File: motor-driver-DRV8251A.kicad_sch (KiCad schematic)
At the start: 7 parts, among them U3 DRV8251ADDAR, U4 INA139

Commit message: minor improvements
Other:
- note added: "DRV8251A Datasheet (driver): https://www.ti.com/lit/ds/symlink/drv8251a.pdf"
- note added: "Drive all motors using PWM signals. Additionally amplify the current sense value to something an ESP32 can measure. Capacitance values are taken directly from the datasheet."
- note added: "INA139 Datasheet (amplifier): https://www.ti.com/lit/ds/symlink/ina139.pdf"
- note added: "Motor Power Section"
- note added: "We assume 4 A max current, since the DRV8251A is rated for 4.1 A. So, a 10 milli-ohm resistor gives us a 40 mV drop. This is then amplified 24 times using a 24k resistor, giving us a theoretical voltage drop of 960 mV. The ESP32 has been tested to measure reliably up to 1 V on its built-in ADC. Resistor power lost = 160 mW."
- company: (none) -> Anuj Verma
- title: (none) -> DRV8251 Motor Driver
- moved on the sheet: C2, C3, C4, R17, R18, U3, U4

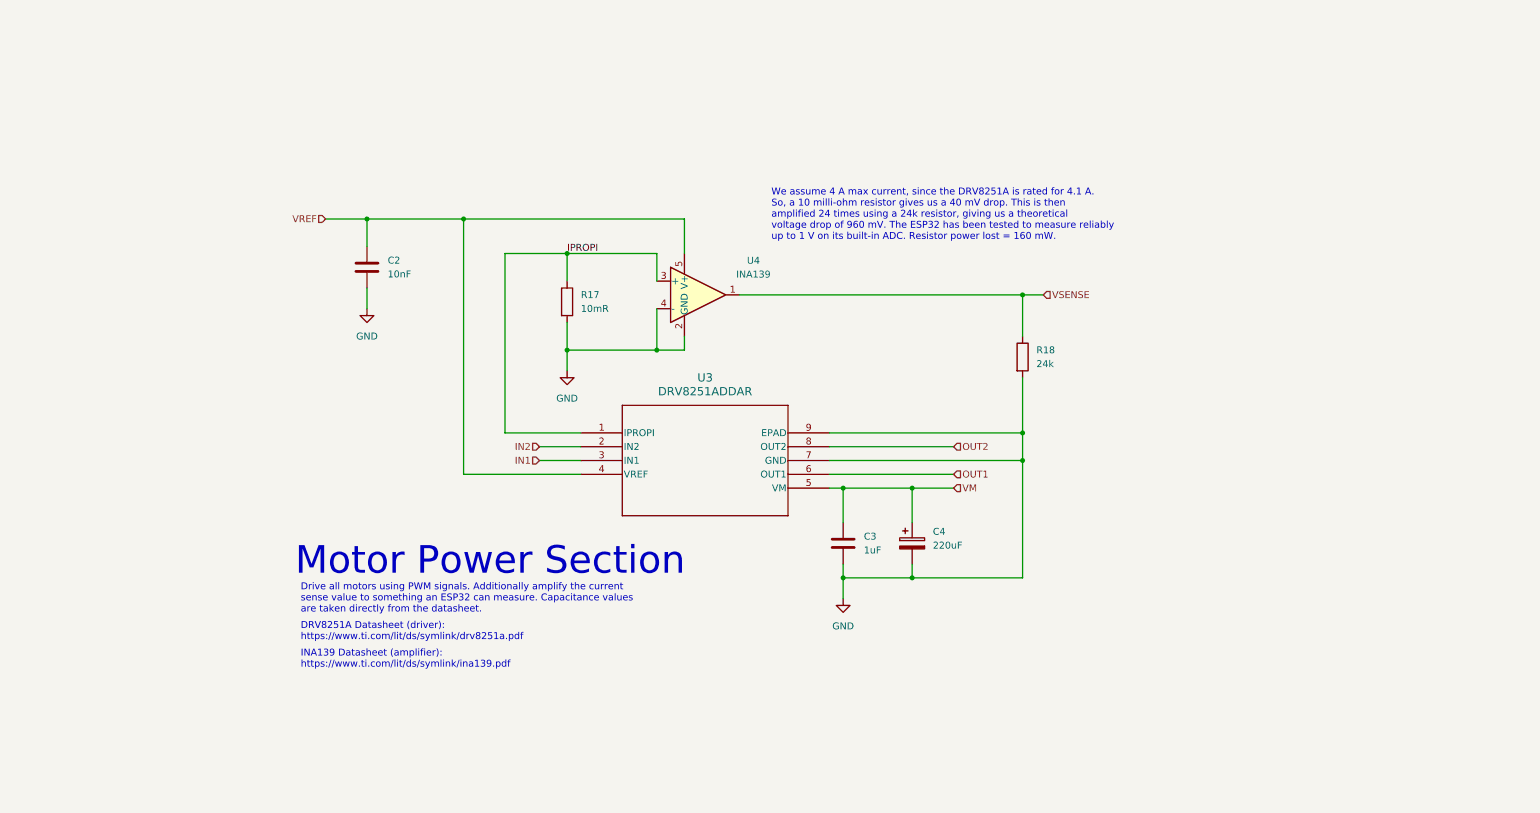
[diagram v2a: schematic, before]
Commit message: basic redesign. PCB not up to date
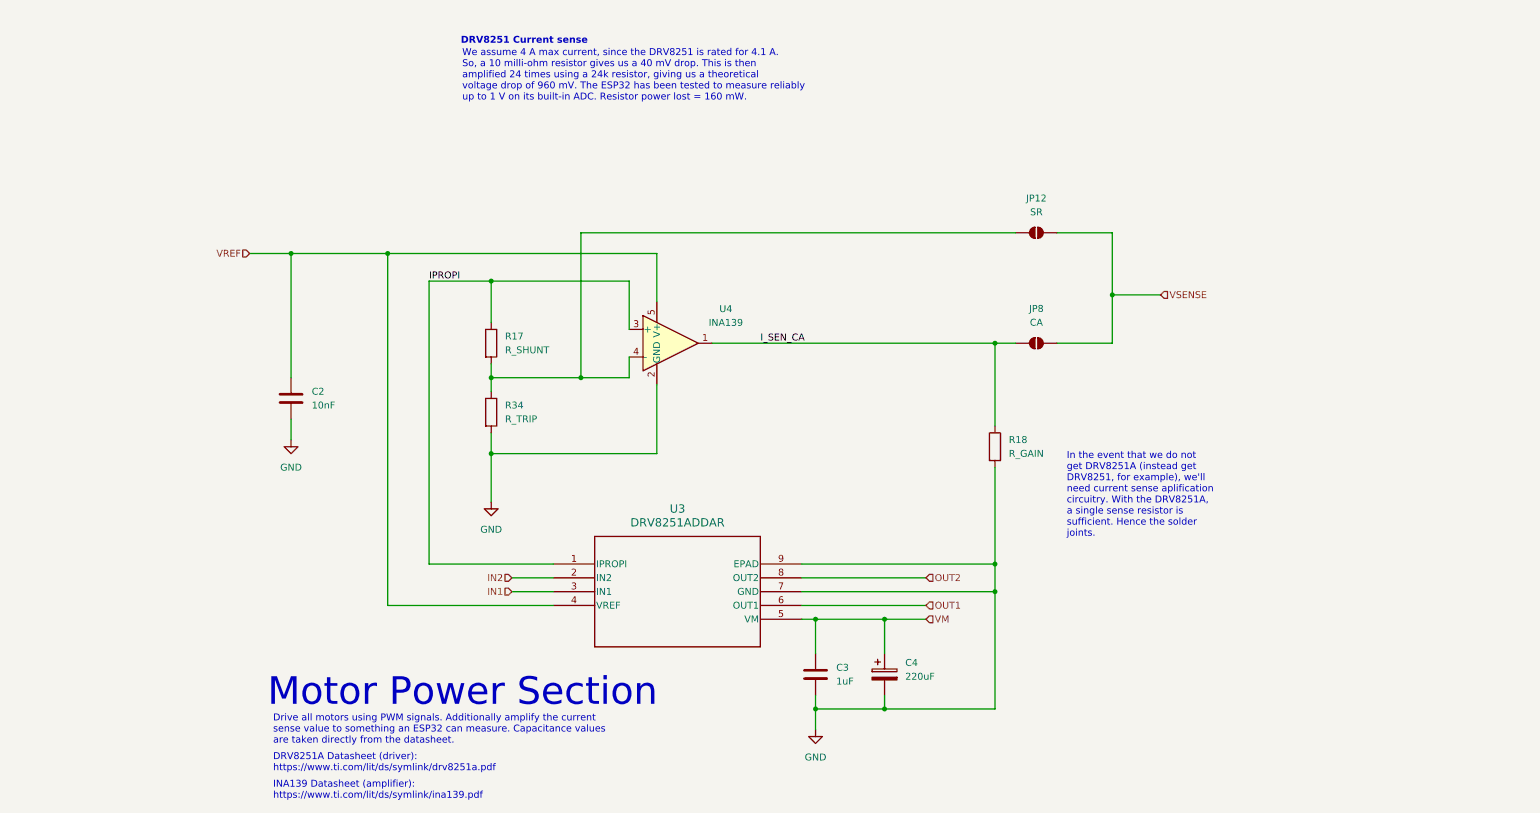
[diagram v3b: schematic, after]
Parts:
- added JP12: SR, Jumper:SolderJumper-2_P1.3mm_Open_Pad1.0x1.5mm, symbol Jumper:SolderJumper_2_Open
- added JP8: CA, Jumper:SolderJumper-2_P1.3mm_Open_Pad1.0x1.5mm, symbol Jumper:SolderJumper_2_Open
- added R34: R_TRIP, Resistor_SMD:R_1206_3216Metric_Pad1.30x1.75mm_HandSolder, symbol Device:R
- R17: value 10mR -> R_SHUNT
- R18: value 24k -> R_GAIN
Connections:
- net GND: now also R34.2; no longer R17.2, U4.4 (-)
- net VSENSE: now also JP12.2 (B), JP8.2 (B); no longer R18.1, U4.1
- new net: JP12.1 (A), R17.2, R34.1, U4.4 (-)
- new net I_SEN_CA: JP8.1 (A), R18.1, U4.1
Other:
- note added: "DRV8251 Current sense"
- note added: "In the event that we do not get DRV8251A (instead get DRV8251, for example), we'll need current sense aplification circuitry. With the DRV8251A, a single sense resistor is sufficient. Hence the solder joints."
- note added: "We assume 4 A max current, since the DRV8251 is rated for 4.1 A. So, a 10 milli-ohm resistor gives us a 40 mV drop. This is then amplified 24 times using a 24k resistor, giving us a theoretical voltage drop of 960 mV. The ESP32 has been tested to measure reliably up to 1 V on its built-in ADC. Resistor power lost = 160 mW."
- note removed: "We assume 4 A max current, since the DRV8251A is rated for 4.1 A. So, a 10 milli-ohm resistor gives us a 40 mV drop. This is then amplified 24 times using a 24k resistor, giving us a theoretical voltage drop of 960 mV. The ESP32 has been tested to measure reliably up to 1 V on its built-in ADC. Resistor power lost = 160 mW."
- moved on the sheet: C2, C3, C4, R17, R18, U3, U4

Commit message: finally done?
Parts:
- renumbered JP12 to JP13, JP8 to JP9, R34 to R35
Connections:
- net I_SEN_CA: now also JP9.2 (B); no longer JP9.1 (A)
- net VSENSE: now also JP9.1 (A); no longer JP9.2 (B)
- net I_SEN_SR: now reaches JP13.1 (A), R17.2, R35.1, U4.4 (-)
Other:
- note added: "ASSUMED OR KNOWN VALUES"
- note added: "CALCULATED VALUES"
- note added: "Drive all motors using PWM signals. Additionally amplify the current sense value to something an ESP32 can measure. Capacitance values are taken directly from the datasheet. Allow option to choose between current measurement with only a shunt resistor, or a shunt resistor and a current-sense amplifier. Depends on the DRV IC chosen. Use the shunt-resistor only (SR), when the DRV IC has IPROPI (e.g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"
- note removed: "DRV8251 Current sense"
- note removed: "Drive all motors using PWM signals. Additionally amplify the current sense value to something an ESP32 can measure. Capacitance values are taken directly from the datasheet."
- note removed: "We assume 4 A max current, since the DRV8251 is rated for 4.1 A. So, a 10 milli-ohm resistor gives us a 40 mV drop. This is then amplified 24 times using a 24k resistor, giving us a theoretical voltage drop of 960 mV. The ESP32 has been tested to measure reliably up to 1 V on its built-in ADC. Resistor power lost = 160 mW."
- moved on the sheet: C2, C3, C4, JP13, JP9, R17, R18, R35, U3, U4
